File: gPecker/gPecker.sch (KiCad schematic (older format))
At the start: 23 parts, among them J1 Conn_02x03_Odd_Even, J1 USB_B_Mini, J2 Conn_01x04_Male, SW1 RESET, U1 LDK130PU33R_DFN6, U2 STM32F103C8Tx

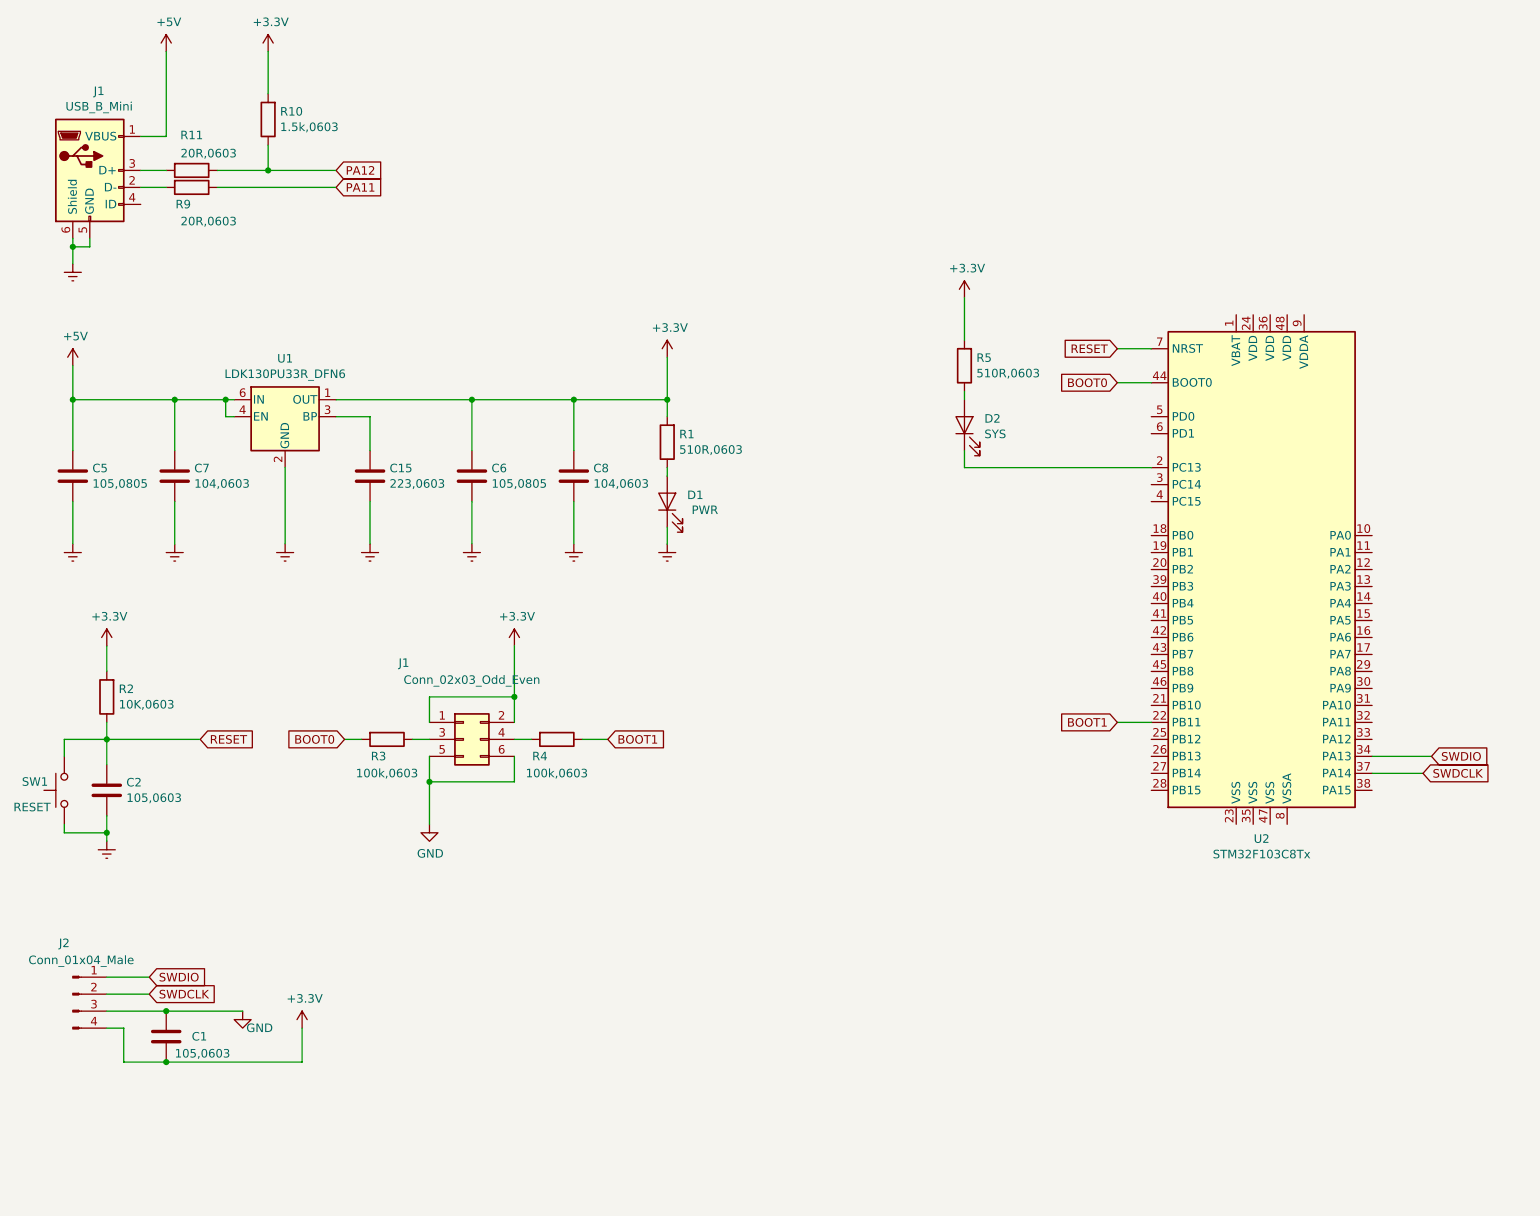
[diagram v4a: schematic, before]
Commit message: add HSE,filter for Digital Voltage..
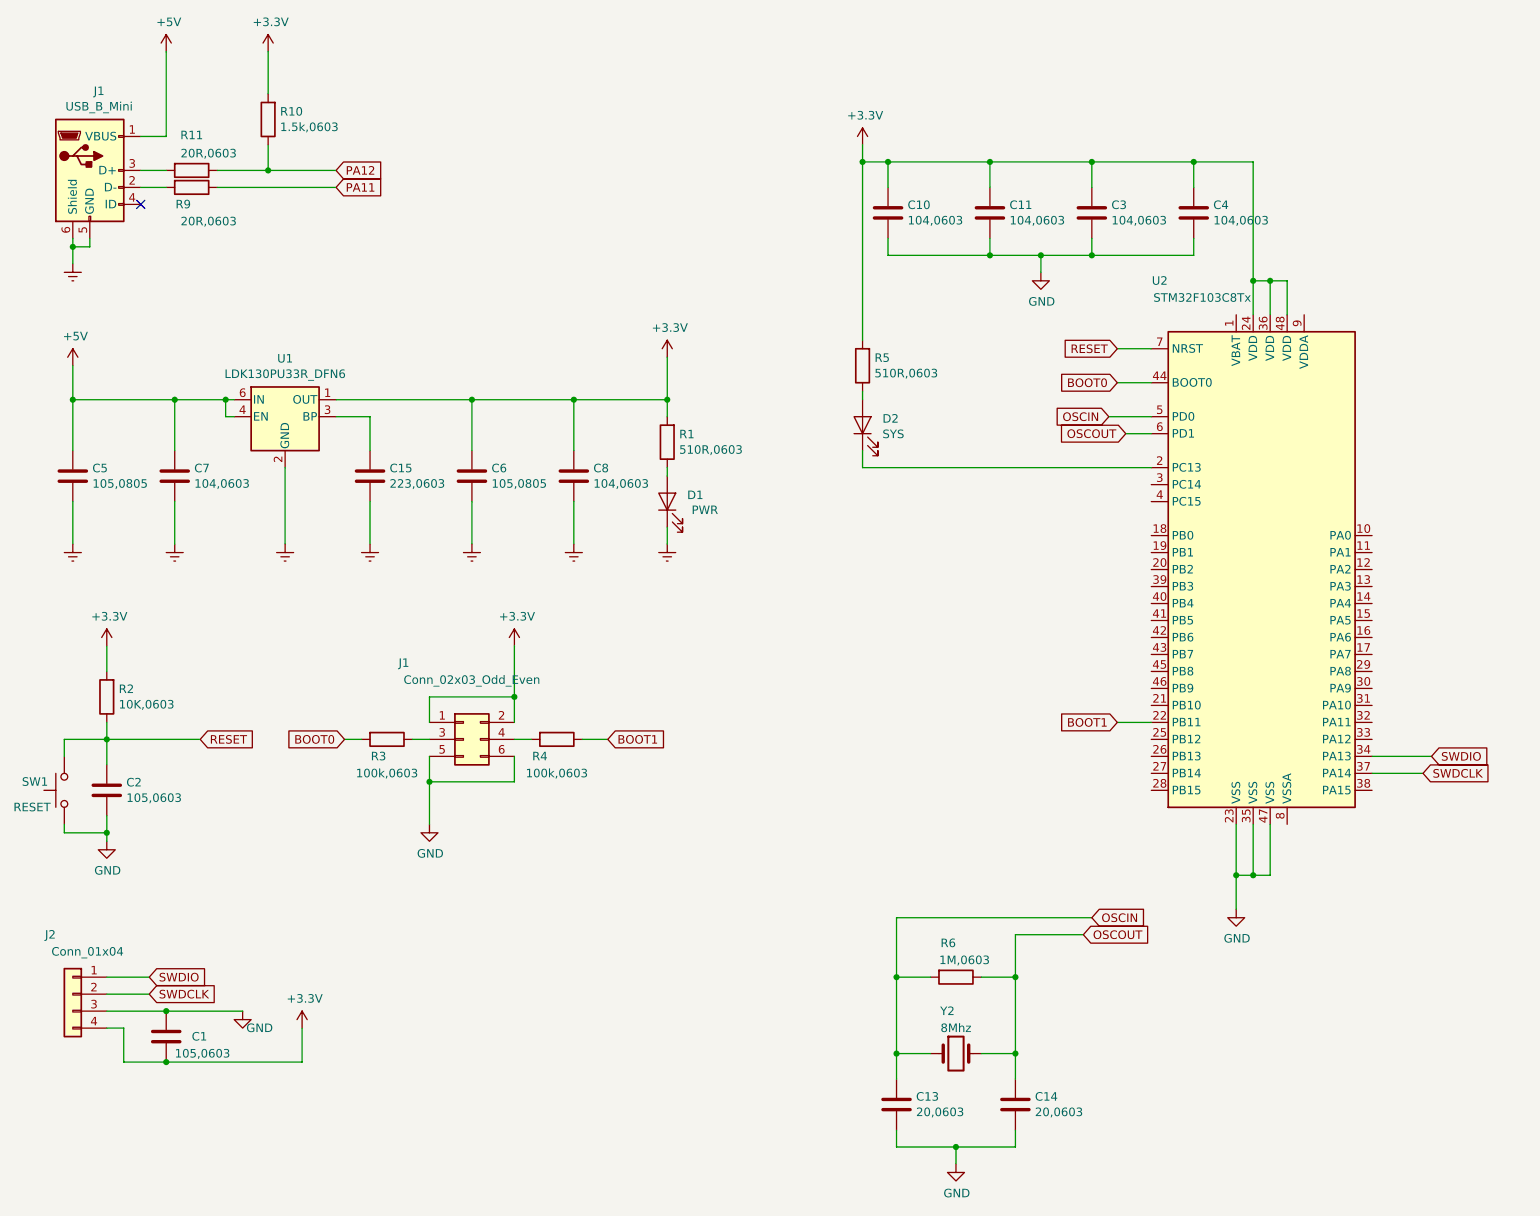
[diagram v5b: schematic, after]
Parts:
- removed J2: Conn_01x04_Male, symbol Connector:Conn_01x04_Male
- added C10, C11, C3, C4: 104,0603, symbol Device:C
- added C13, C14: 20,0603, symbol Device:C
- added J2: Conn_01x04, symbol Connector_Generic:Conn_01x04
- added R6: 1M,0603, symbol Device:R
- added Y2: 8Mhz, symbol Device:Crystal
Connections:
- net +3V3: now also U2.24 (VDD), U2.36 (VDD), U2.48 (VDD), C10.1, C11.1, C3.1, C4.1, J2.4 (Pin_4)
- net Earth: no longer C2.2, SW1.1
- net GND: now also C2.2, SW1.1, U2.23 (VSS), U2.35 (VSS), U2.47 (VSS), C10.2, C11.2, C13.2, C14.2, C3.2, C4.2, J2.3 (Pin_3)
- net SWDCLK: now also J2.2 (Pin_2)
- net SWDIO: now also J2.1 (Pin_1)
- net OSCIN: now reaches U2.5 (PD0)
- net OSCIN: now also C13.1, R6.2, Y2.1
- net OSCOUT: now reaches U2.6 (PD1)
- net OSCOUT: now also C14.1, R6.1, Y2.2
- no-connect marks 0 -> 1
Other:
- moved on the sheet: D2, R5
